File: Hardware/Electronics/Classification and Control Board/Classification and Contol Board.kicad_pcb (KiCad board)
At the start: 4 copper layers, 53.9 x 62.3 mm, 94 parts, among them J1 SWD Header, J10 USB_B_Mini, J2 Barrel_Jack, J3 Thumb, J4 Index, J5 Middle, J6 Ring, J7 Pinky, J8 Wrist, J9 HC05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

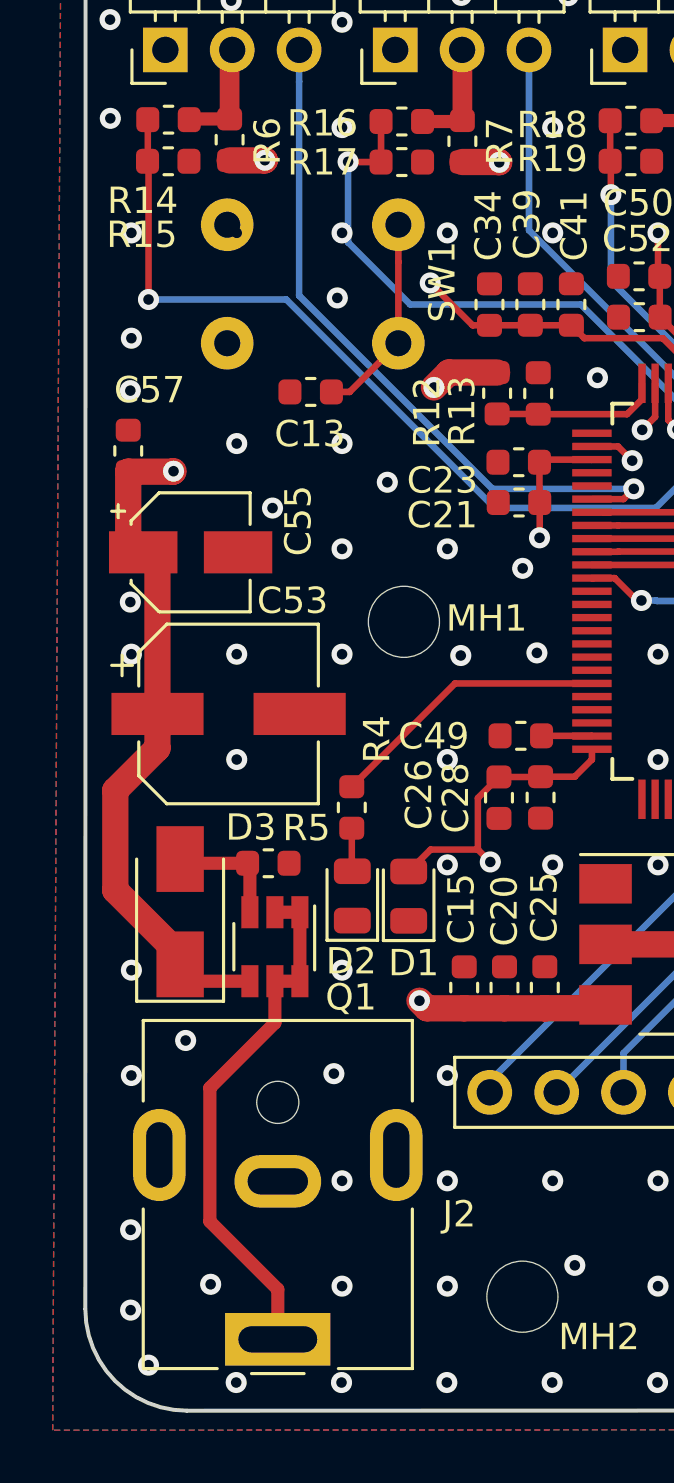
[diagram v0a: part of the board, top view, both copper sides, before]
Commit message: Pushed power connector back, created Production PDFs
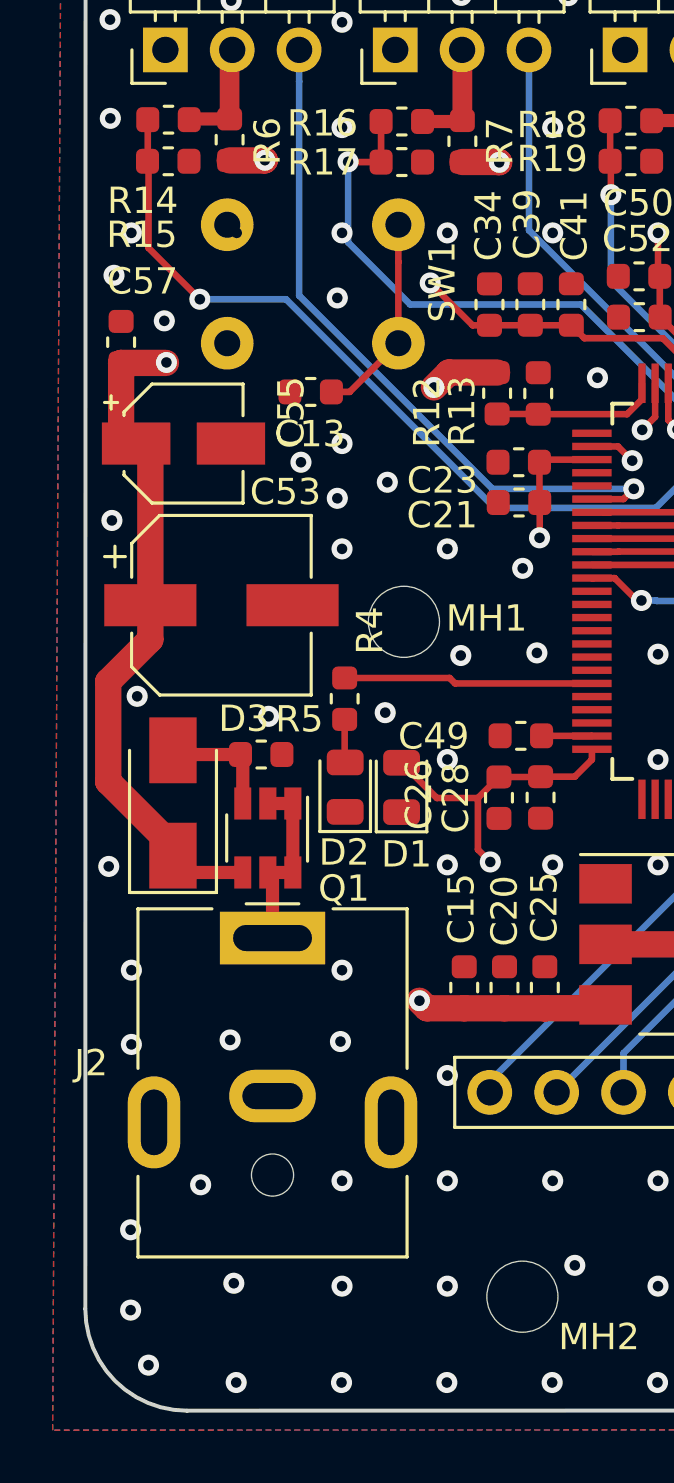
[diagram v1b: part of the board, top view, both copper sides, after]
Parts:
- moved J2 15.2 mm to (121.5, 105.6), turned to 0 degrees
- moved D2 4.14 mm to (124.3, 99.9)
- moved R4 4.14 mm to (124.3, 96.5)
- moved C53 4.14 mm to (119.6, 93.0)
- moved C55 4.14 mm to (118.2, 86.8)
- moved C57 4.14 mm to (115.8, 83.0)
- moved D1 4.14 mm to (126.4, 99.9)
- moved D3 4.14 mm to (117.8, 100.5)
- moved Q1 4.14 mm to (121.4, 101.8)
- moved R5 4.14 mm to (121.1, 98.6)
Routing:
- net Net-(J2-Pad1): track 20.3 -> 7.08 mm
- net /V+: track 52.7 -> 50.1 mm
- net Net-(R4-Pad1): track 10.7 -> 9.48 mm
- net /Control/FB1: track 35.6 -> 34.4 mm
- net (no net): vias 0 -> 1

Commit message: DRC passes
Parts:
- moved C21 1.17 mm to (129.9, 89.7)
- moved C23 1.17 mm to (129.9, 88.1)
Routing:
- net /STM32F407VGTx/PWM1: track 26.8 -> 23.7 mm
- net /GND: track 20.6 -> 22.6 mm, vias 164 -> 162
- net /STM32F407VGTx/3V3: track 86.5 -> 87.8 mm
- net /STM32F407VGTx/PWM2: track 24.8 -> 25.9 mm
- net /Control/FB1: track 34.4 -> 35.2 mm
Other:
- net class 0.5mm: clearance 0.2 -> 0.15
- net class 1mm: clearance 0.2 -> 0.15
- net class Default: clearance 0.2 -> 0.15
- rule trace_clearance: 0.2 -> 0.15

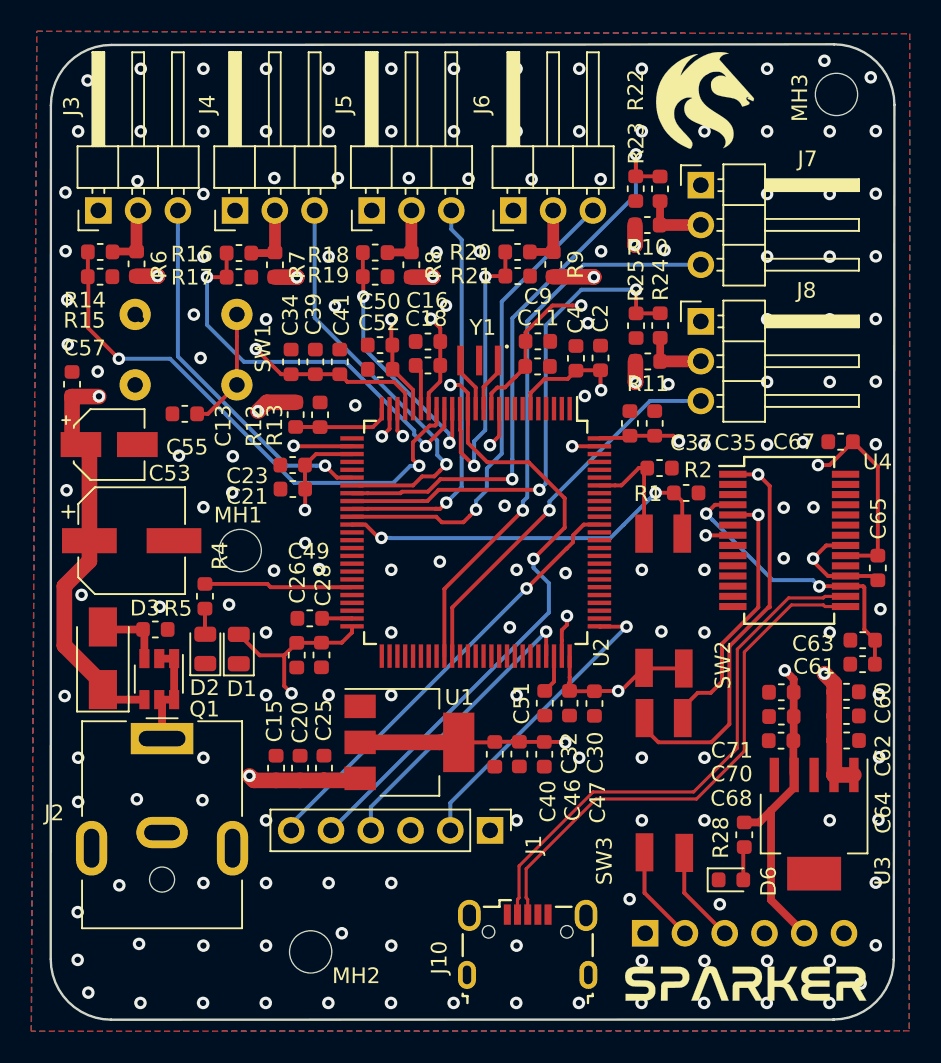
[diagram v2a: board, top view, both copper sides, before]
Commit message: Removed BT / USB switch, changed reset button switch so now it will be correct
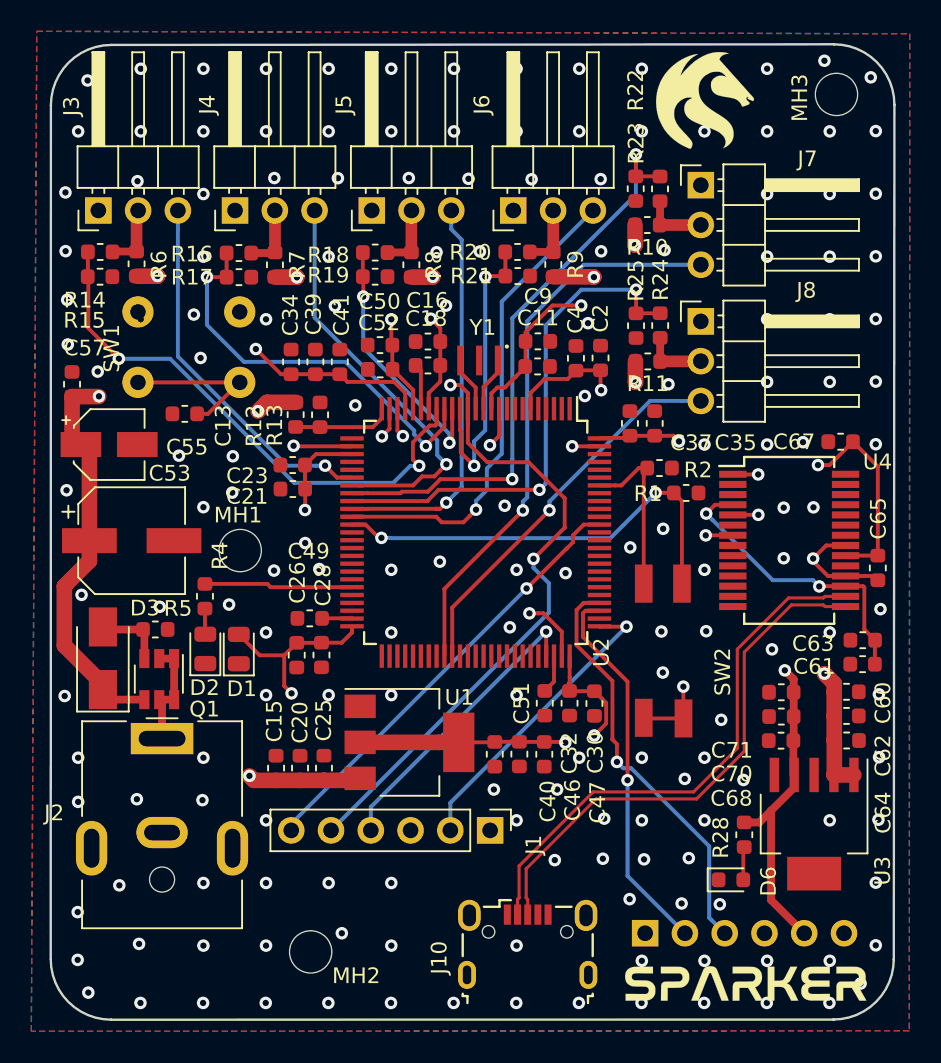
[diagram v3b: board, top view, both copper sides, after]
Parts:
- removed SW3: BT Enable, Switches:DIP-Switch_01x02
- moved SW1 7.85 mm to (120.0, 78.4), turned to 0 degrees
- moved SW2 3.19 mm to (154.8, 95.7)
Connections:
- J9 pad 2: Net-(J9-Pad2) -> /Communications/BT_TX
- J9 pad 3: Net-(J9-Pad3) -> /Communications/BT_RX
- U2 pad 78: Net-(U2-Pad78) -> /Communications/BT_TX
- U2 pad 79: Net-(U2-Pad79) -> /Communications/BT_RX
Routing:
- net /Communications/BT_RX: track 0.00 -> 26.5 mm, vias 0 -> 1
- net /Communications/BT_TX: track 0.00 -> 24.3 mm, vias 0 -> 1
- net /Communications/TX: track 57.2 -> 33.0 mm
- net /Communications/RX: track 50.8 -> 35.3 mm
- net Net-(J9-Pad2): track 6.50 -> 0.00 mm
- net Net-(J9-Pad3): track 6.20 -> 0.00 mm
- net /STM32F407VGTx/BOOT0: track 7.79 -> 11.3 mm
- net /STM32F407VGTx/BOOT1: track 25.0 -> 28.2 mm
- net /STM32F407VGTx/NRST: track 62.0 -> 63.9 mm
- net /STM32F407VGTx/3V3: track 87.8 -> 89.5 mm, vias 10 -> 11
- net /GND: track 22.6 -> 24.0 mm, vias 162 -> 176
